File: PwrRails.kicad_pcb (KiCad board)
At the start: 2 copper layers, 99 parts, among them IC1 ATMEGA8-AI, P1 CONN_01X02, P10 CONN_01X02, P11 CONN_01X03, P12 PR 5V, P13 PR 5V, P2 PR 5V, P3 CONN_01X02, P4 CONN_01X05, P5 CONN_01X01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

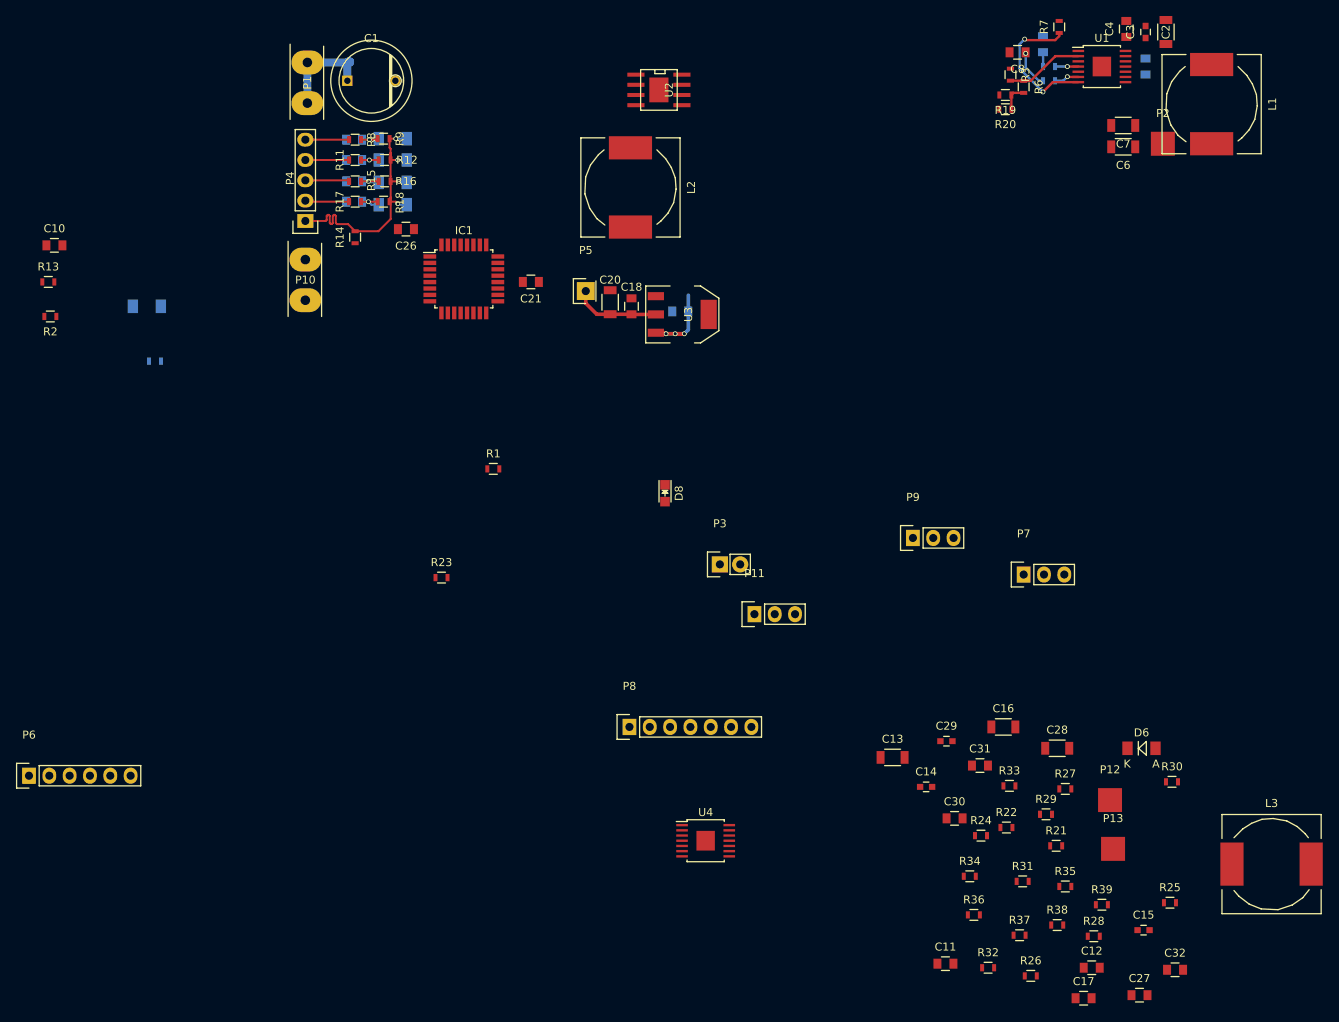
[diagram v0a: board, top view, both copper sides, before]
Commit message: 12V Seite fast fertig
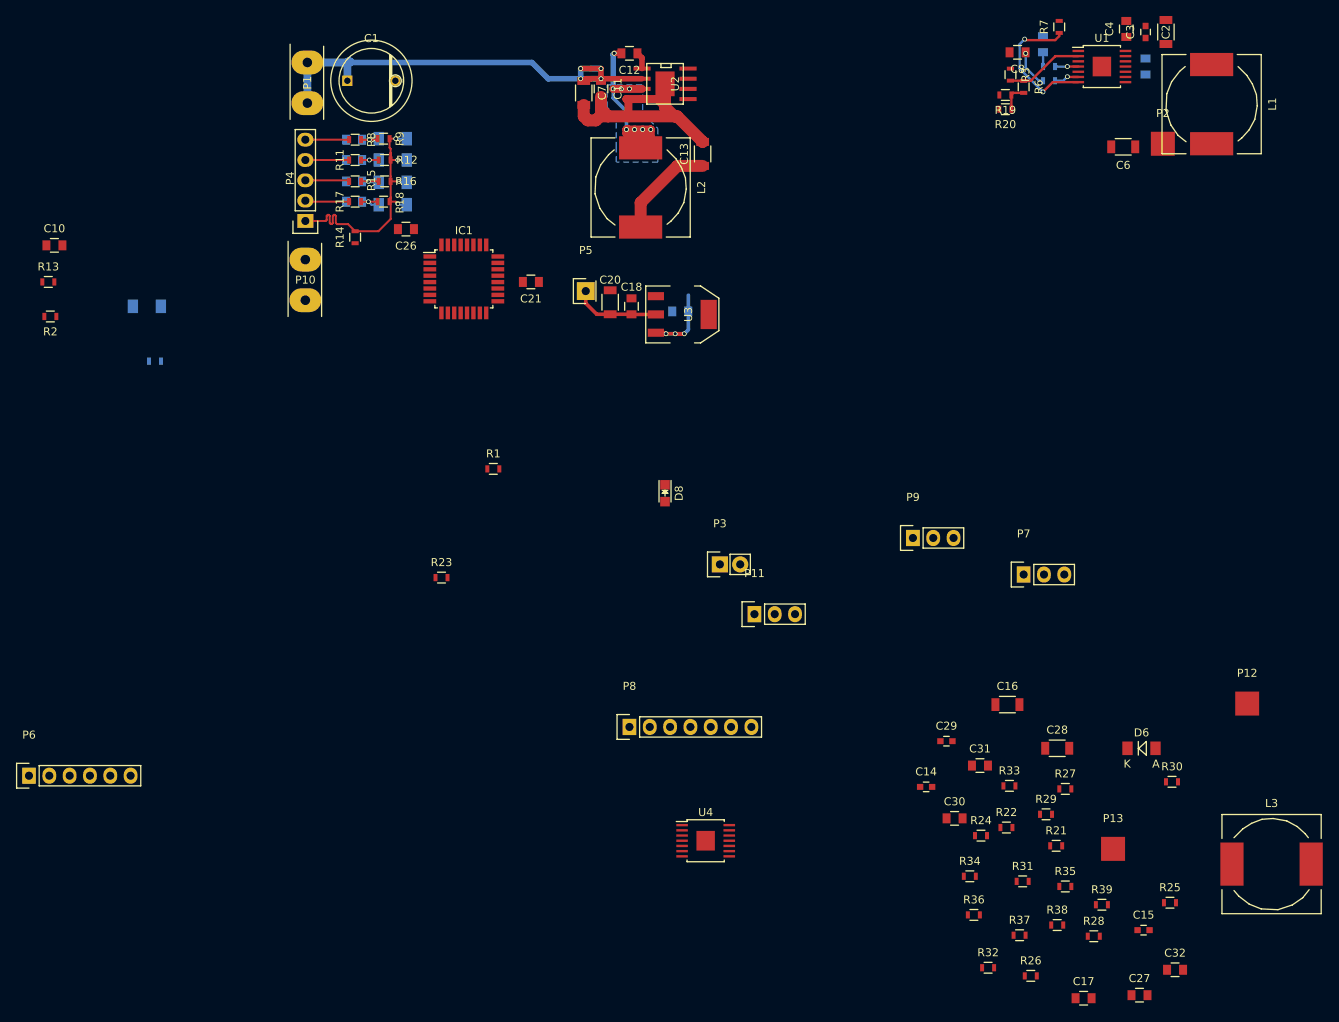
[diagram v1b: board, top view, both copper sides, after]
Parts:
- moved C12 128.1 mm to (166.8, 41.0), turned to 180 degrees
- moved C11 117.5 mm to (163.2, 45.5), turned to 270 degrees
- moved C13 79.1 mm to (175.9, 53.6), turned to 90 degrees
- moved C7 67.6 mm to (161.0, 46.0), turned to 270 degrees
- moved P12 21.0 mm to (244.0, 122.3)
- moved C16 2.84 mm to (214.0, 122.4)
- moved L2 1.27 mm to (168.1, 57.8)
- moved U2 1.08 mm to (171.2, 44.8)
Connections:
- net Net-(C12-Pad2) renamed /Switch_12V
- C27 pad 1: /Switch_5V -> /Switch_3V
- C29 pad 1: /VFB_5V -> /VFB_3V
- L3 pad 1: /Switch_5V -> /Switch_3V
- R31 pad 2: /VFB_5V -> /VFB_3V
- R34 pad 1: /VFB_5V -> /VFB_3V
- U4 pad 10: /Switch_5V -> /Switch_3V
- U4 pad 11: /Switch_5V -> /Switch_3V
- U4 pad 2: /VFB_5V -> /VFB_3V
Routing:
- net /Switch_12V: track 0.00 -> 51.0 mm, vias 0 -> 8
- net AkkuIn: track 13.2 -> 63.9 mm, vias 0 -> 4
- net GND: track 0.00 -> 32.9 mm
- net +12V: track 15.4 -> 28.1 mm
- net Net-(C12-Pad1): track 0.00 -> 2.14 mm
- added copper zone on B.Cu, net /Switch_12V
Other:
- rule pad_to_mask_clearance: 0.2 -> 0.1

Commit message: PCB quasi fertig!
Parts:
- added C33: 1µ, Capacitors_SMD:C_0805, F.Cu at (209.4, 77.2)
- added Q1: Q_PMOS_GSD, TO_SOT_Packages_SMD:SOT-23, F.Cu at (207.5, 62.4)
- added R40: R, Resistors_SMD:R_0603, F.Cu at (212.9, 66.5)
- added R41: R, Resistors_SMD:R_0603, F.Cu at (214.0, 71.9)
- added R42: R, Resistors_SMD:R_0603, F.Cu at (212.1, 71.9)
- added R43: R, Resistors_SMD:R_0603, F.Cu at (212.1, 69.1)
- added U5: LM293, SMD_Packages:SOIC-8-N, F.Cu at (208.4, 68.2)
- added U6: NCP51460, TO_SOT_Packages_SMD:SOT-23, F.Cu at (209.3, 74.3)
- added X1: CRYSTAL_SMD, Toni:CerOsc_3,2x1,3, F.Cu at (140.0, 70.1)
- C16, C2: footprint Capacitors_SMD:C_1206 -> Capacitors_SMD:C_1210
- C32, D6, P12, P13, P2, R2, R24, R39: moved to B.Cu
- C5, C9, R10, R4, R5: moved to F.Cu
- L1: footprint Inductors_NEOSID:Neosid_Inductor_SM-NE127 -> Z_Borus_SRN8040
- L3: footprint Inductors_NEOSID:Neosid_Inductor_SM-NE127 -> Z_Coilcraft_XFL4020
- P6: footprint Socket_Strips:Socket_Strip_Straight_1x06 -> Socket_Strips:Socket_Strip_Straight_2x03
- P8: footprint Socket_Strips:Socket_Strip_Straight_1x07 -> Socket_Strip_BIG_1x07
- moved C32 122.0 mm to (152.3, 65.9)
- moved R26 121.7 mm to (176.7, 41.5)
- moved C15 118.8 mm to (179.2, 43.7)
- moved R25 115.0 mm to (176.9, 47.5), turned to 90 degrees
- moved R28 113.5 mm to (179.2, 47.5), turned to 90 degrees
- moved R39 111.3 mm to (152.0, 64.1), turned to 180 degrees
- moved R30 106.0 mm to (179.5, 41.5)
- moved R21 101.9 mm to (189.2, 42.9), turned to 90 degrees
- moved R27 98.8 mm to (176.8, 44.7), turned to 90 degrees
- moved C17 98.0 mm to (193.0, 66.0), turned to 180 degrees
- moved C27 96.3 mm to (197.5, 68.3), turned to 180 degrees
- moved P8 96.1 mm to (221.2, 46.1), turned to 270 degrees
- moved R29 94.2 mm to (179.2, 50.7), turned to 90 degrees
- moved R37 93.2 mm to (184.4, 63.4)
- moved P12 93.1 mm to (175.3, 59.4)
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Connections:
- D1 pad 2: AGND -> GND
- D2 pad 2: AGND -> GND
- D3 pad 2: AGND -> GND
- D4 pad 2: AGND -> GND
- D5 pad 2: AGND -> GND
- D6 pad 2: AGND -> GND
- P8 pad 5: +3V3 -> Switched_3V3
- R22 pad 2: +3V3 -> +12V
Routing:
- net GND: track 32.9 -> 614.3 mm, vias 0 -> 191
- net AkkuIn: track 63.9 -> 330.4 mm, vias 4 -> 13
- net +5V: track 0.00 -> 238.6 mm, vias 0 -> 15
- net +12V: track 28.1 -> 195.0 mm, vias 3 -> 13
- net +3V3: track 0.00 -> 101.8 mm, vias 0 -> 10
- net /ADC7: track 0.00 -> 62.2 mm, vias 0 -> 4
- net /Switch_12V: track 51.0 -> 12.6 mm, vias 8 -> 4
- net /ADC4: track 0.00 -> 34.9 mm, vias 0 -> 4
- net AGND: track 35.3 -> 68.9 mm
- net /ADC6: track 0.00 -> 29.2 mm, vias 0 -> 3
- net /ADC0: track 4.24 -> 31.0 mm, vias 1 -> 2
- net Net-(IC1-Pad12): track 0.00 -> 25.6 mm, vias 0 -> 1
- net Net-(IC1-Pad30): track 0.00 -> 24.0 mm
- net Net-(IC1-Pad13): track 0.00 -> 23.8 mm, vias 0 -> 1
- net /ADC1: track 4.26 -> 27.3 mm, vias 1 -> 2
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- added copper zone on F.Cu, net +3V3
- added copper zone on F.Cu, net +5V
- added copper zone on F.Cu, net /Switch_12V
- added copper zone on F.Cu, net /Switch_3V
- added copper zone on F.Cu, net /Switch_5V
- added copper zone on F.Cu, net AkkuIn
- added copper zone on B.Cu, net GND
- added copper zone on F.Cu, net GND
- removed copper zone on B.Cu, net /Switch_12V
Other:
- board outline added: 101.6 x 44.5 mm

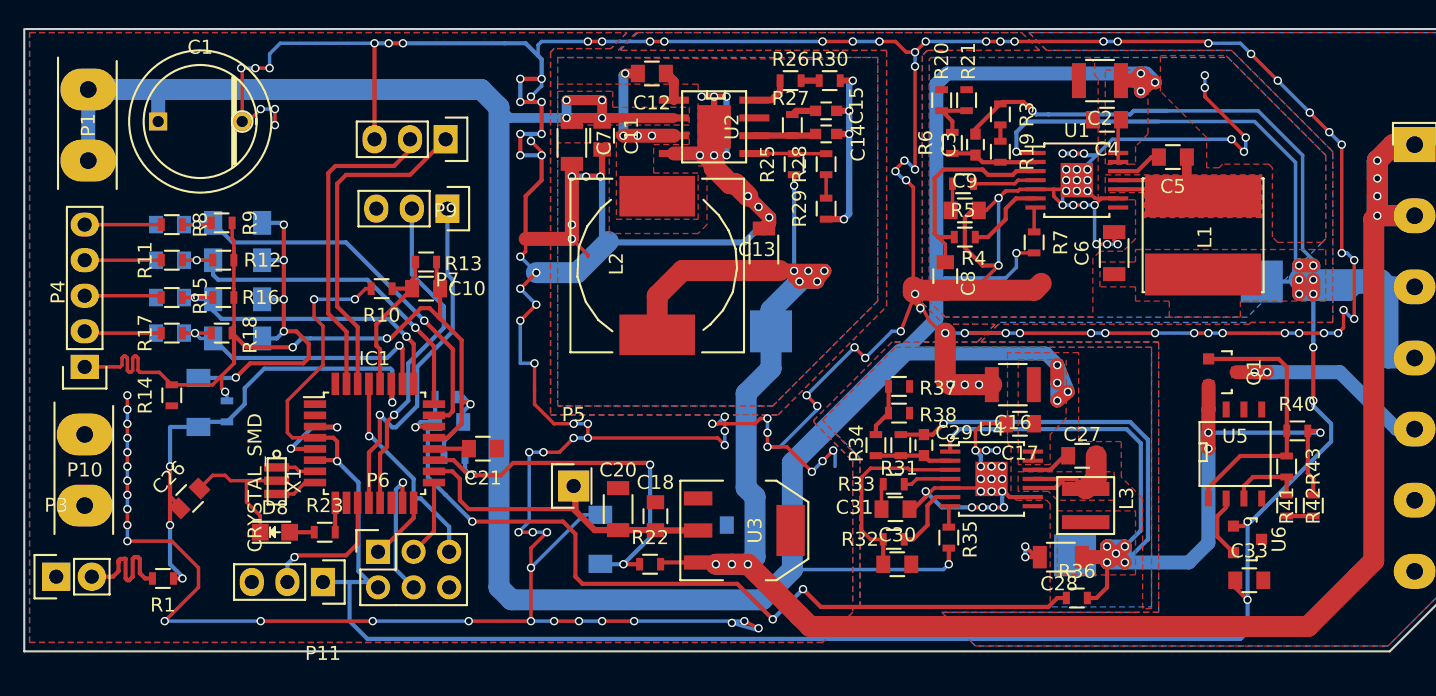
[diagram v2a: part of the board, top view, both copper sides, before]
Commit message: Bohrungen hinzugefügt.
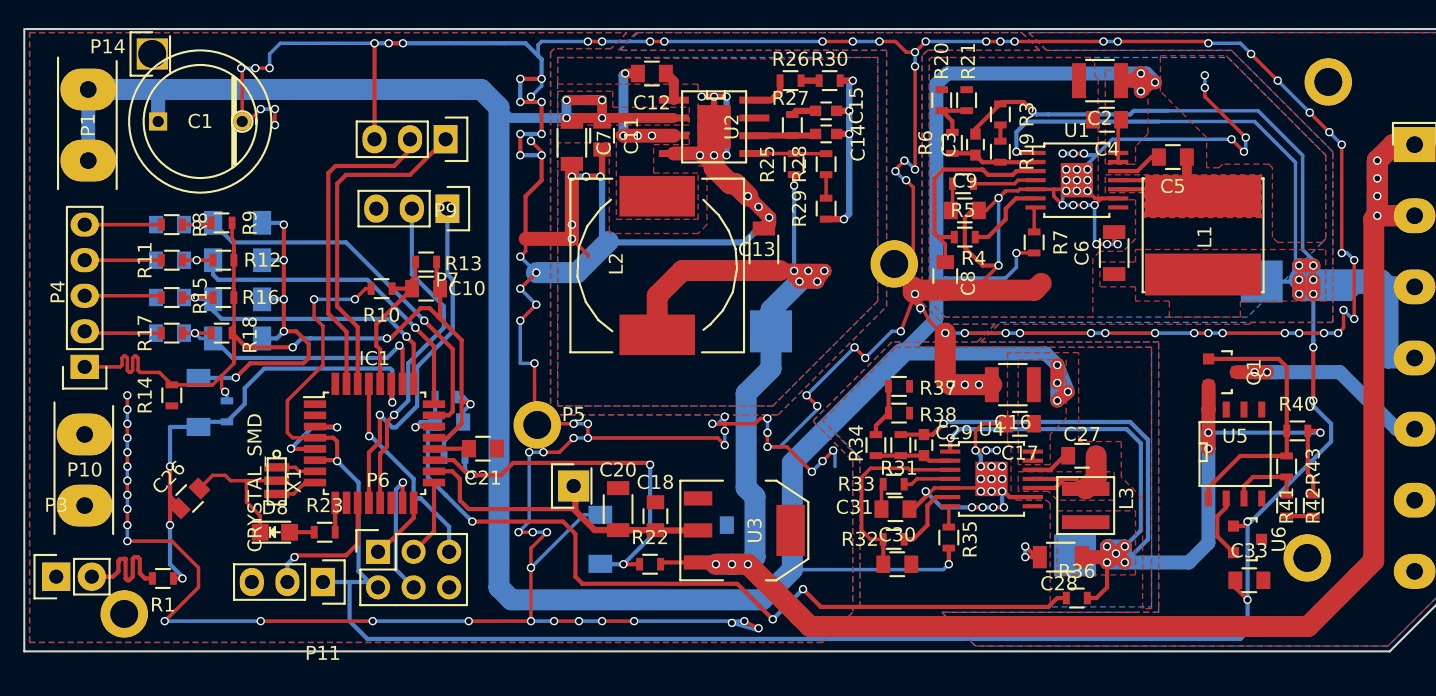
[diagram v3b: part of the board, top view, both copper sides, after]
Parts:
- added P14: CONN_01X01, Z_Schaltwandler_Panel_Bohrungen, F.Cu at (131.1, 39.6)
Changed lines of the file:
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@@
 (kicad_pcb (version 4) (host pcbnew 0.201511171411+6319~30~ubuntu15.10.1-product)
   (general
-    (links 224)
+    (links 228)
     (no_connects 0)
-    (area 0 0 0 0)
+    (area 121.844999 37.770999 223.595001 82.371001)
     (thickness 1.6)
     (drawings 47)
     (tracks 1364)
     (zones 0)
-    (modules 108)
+    (modules 109)
     (nets 74)
   )
@@
   )
   (setup
-    (last_trace_width 0.3)
+    (last_trace_width 0.25)
     (user_trace_width 0.25)
     (user_trace_width 0.3)
@@
     (add_net AkkuIn)
   )
+  (module Z_Schaltwandler_Panel_Bohrungen (layer F.Cu)
+    (at 131.064 39.624)
+    (descr "Through hole socket strip")
+    (tags "socket strip")
+    (fp_text reference P14 (at -3.175 -0.508) (layer F.SilkS)
+      (effects (font (size 1 1) (thickness 0.15)))
+    )
+    (fp_text value CONN_01X01 (at 0 -3.1) (layer F.Fab)
+      (effects (font (size 1 1) (thickness 0.15)))
+    )
+    (fp_line (start -1.75 -1.75) (end -1.75 1.75) (layer F.CrtYd) (width 0.05))
+    (fp_line (start 1.75 -1.75) (end 1.75 1.75) (layer F.CrtYd) (width 0.05))
+    (fp_line (start -1.75 -1.75) (end 1.75 -1.75) (layer F.CrtYd) (width 0.05))
+    (fp_line (start -1.75 1.75) (end 1.75 1.75) (layer F.CrtYd) (width 0.05))
+    (fp_line (start 1.27 1.27) (end 1.27 -1.27) (layer F.SilkS) (width 0.15))
+    (fp_line (start -1.55 -1.55) (end 0 -1.55) (layer F.SilkS) (width 0.15))
+    (fp_line (start -1.55 -1.55) (end -1.55 1.55) (layer F.SilkS) (width 0.15))
+    (fp_line (start -1.55 1.55) (end 0 1.55) (layer F.SilkS) (width 0.15))
+    (pad 1 thru_hole rect (at 0 0) (size 2.2352 2.2352) (drill 2) (layers *.Cu *.Mask F.SilkS)
+      (net 2 GND))
+    (pad 1 thru_hole circle (at 27.5 26.5) (size 3.4 3.4) (drill 2) (layers *.Cu *.Mask F.SilkS)
+      (net 2 GND))
+    (pad 1 thru_hole circle (at -2 40) (size 3.4 3.4) (drill 2) (layers *.Cu *.Mask F.SilkS)
+      (net 2 GND))
+    (pad 1 thru_hole circle (at 53 15) (size 3.4 3.4) (drill 2) (layers *.Cu *.Mask F.SilkS)
+      (net 2 GND))
+    (pad 1 thru_hole circle (at 84 2) (size 3.4 3.4) (drill 2) (layers *.Cu *.Mask F.SilkS)
+      (net 2 GND) (zone_connect 2))
+    (pad 2 thru_hole circle (at 82.5 36) (size 3.4 3.4) (drill 2) (layers *.Cu *.Mask F.SilkS))
+    (model Socket_Strips.3dshapes/Socket_Strip_Straight_1x01.wrl
+      (at (xyz 0 0 0))
+      (scale (xyz 1 1 1))
+      (rotate (xyz 0 0 180))
+    )
+  )
   (module Toni:CerOsc_3,2x1,3 (layer F.Cu)
     (at 139.954 70.104 270)
@@
     (descr "Radial Electrolytic Capacitor Diameter 8mm x Length 13mm, Pitch 3.8mm")
     (tags "Electrolytic Capacitor")
-    (fp_text reference C1 (at 1.9 -5.3) (layer F.SilkS)
+    (fp_text reference C1 (at 1.905 0) (layer F.SilkS)
       (effects (font (size 1 1) (thickness 0.15)))
     )
@@
       )
     )
+  )
+  (zone (net 0) (net_name "") (layer F.Cu) (hatch edge 0.508)
+    (connect_pads (clearance 0.3))
+    (min_thickness 0.254)
+    (keepout (tracks allowed) (vias allowed) (copperpour not_allowed))
+    (fill (arc_segments 16) (thermal_gap 0.508) (thermal_bridge_width 0.508))
+    (polygon
+      (pts
+        (xy 182.88 56.515) (xy 182.88 52.959) (xy 181.737 52.959) (xy 181.737 56.515)
+      )
+    )
+  )
+  (zone (net 0) (net_name "") (layer B.Cu) (hatch edge 0.508)
+    (connect_pads (clearance 0.3))
+    (min_thickness 0.254)
+    (keepout (tracks allowed) (vias allowed) (copperpour not_allowed))
+    (fill (arc_segments 16) (thermal_gap 0.508) (thermal_bridge_width 0.508))
+    (polygon
+      (pts
+        (xy 182.88 56.515) (xy 182.88 52.832) (xy 181.61 52.832) (xy 181.61 56.515) (xy 182.245 56.515)
+      )
+    )

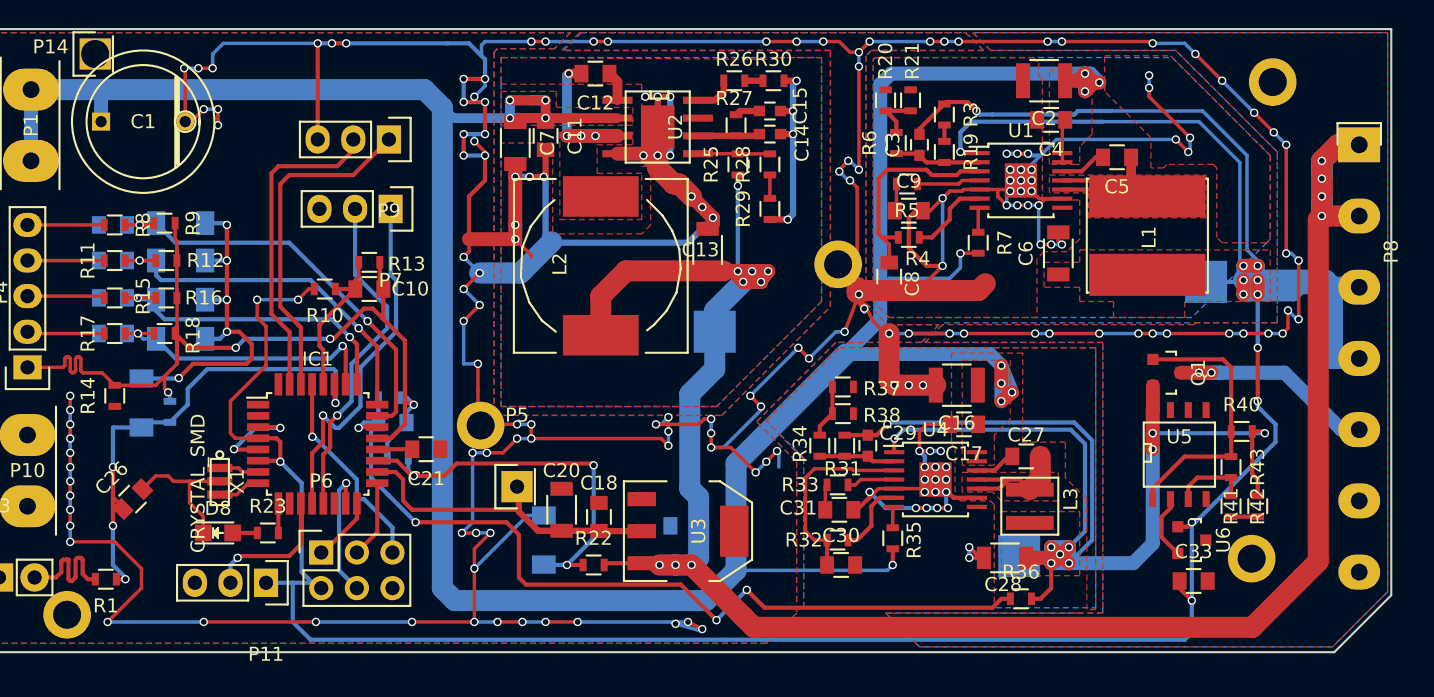
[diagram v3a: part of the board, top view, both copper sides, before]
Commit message: Lötstopp-Auspahrungen und Beschtückungsdruck ist fertig!
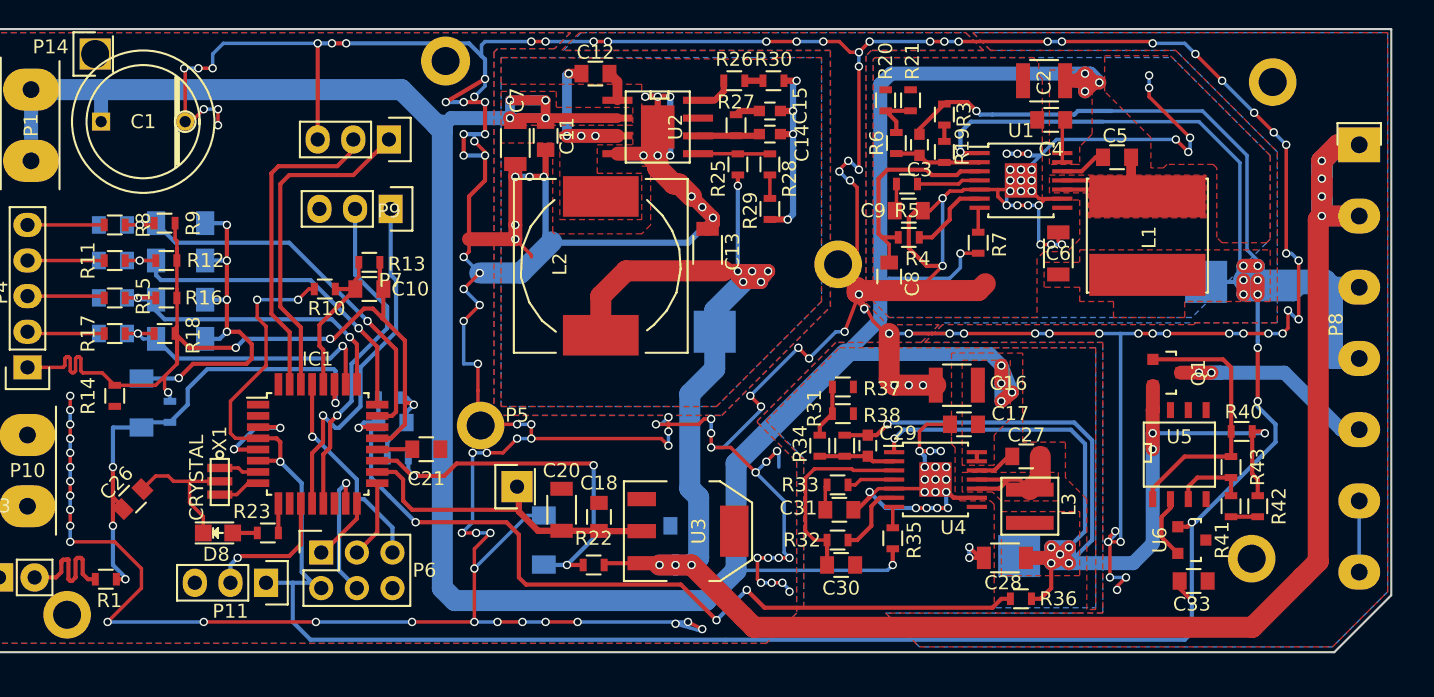
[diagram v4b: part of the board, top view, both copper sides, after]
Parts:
- X1: value CRYSTAL_SMD -> CRYSTAL
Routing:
- net AkkuIn: track 330.4 -> 270.4 mm
- net GND: track 614.3 -> 656.8 mm, vias 191 -> 205
- net /Switch_12V: track 12.6 -> 13.6 mm
